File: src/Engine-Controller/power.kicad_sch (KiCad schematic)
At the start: 32 parts, among them P1 EJ508A, U2 LM22672MRE-5.0_NOPB, U3 LMS8117AMP-3.3_NOPB, U6 TPS2115APWR

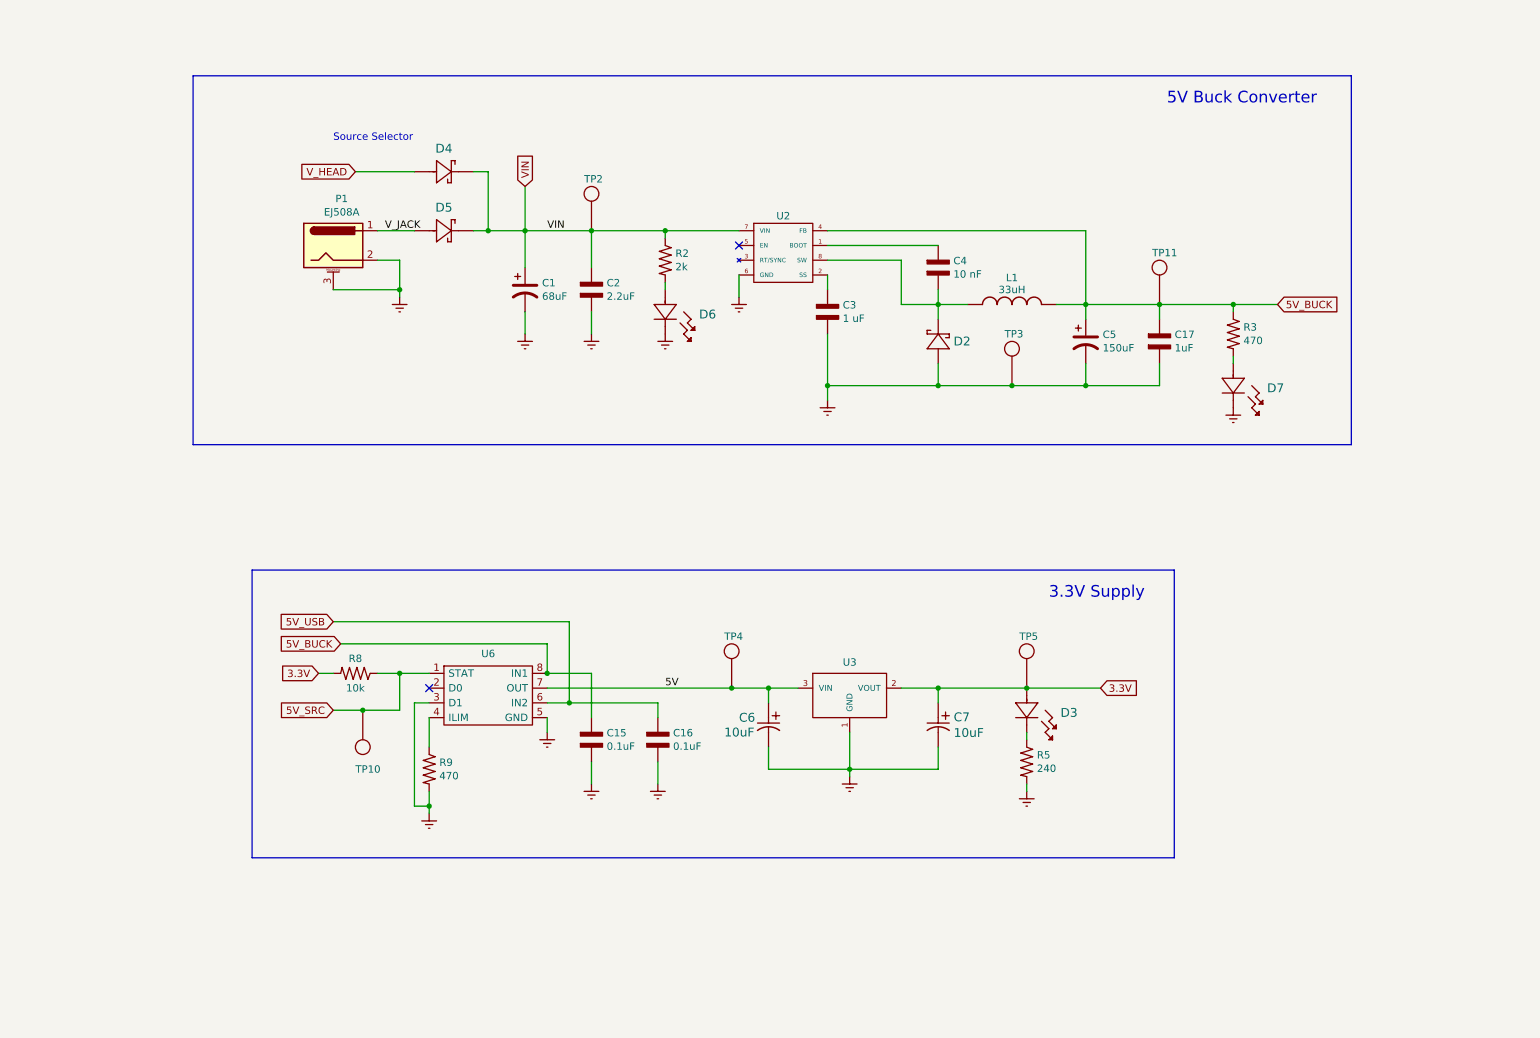
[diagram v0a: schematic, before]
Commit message: Cleaned up power schematic
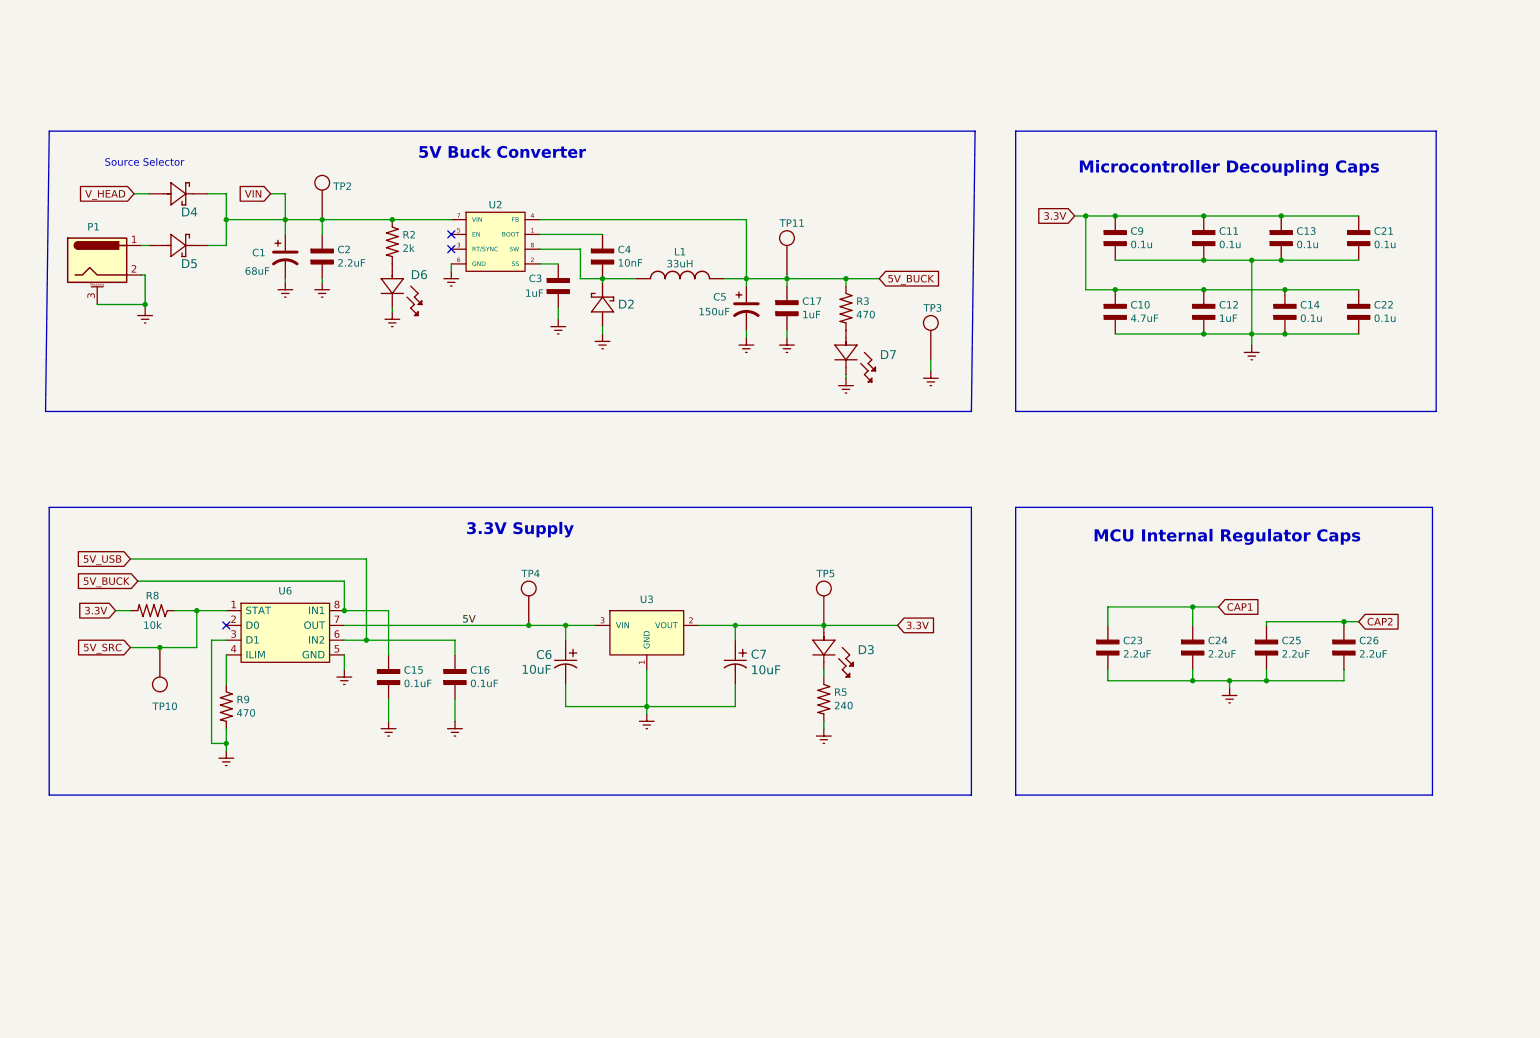
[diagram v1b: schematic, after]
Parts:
- added C10: 4.7uF, Engine-Controller:CAP_0603, symbol Engine-Controller:CAP_0603
- added C11, C13, C14, C21, C22, C9: 0.1u, Engine-Controller:CAP_0603, symbol Engine-Controller:CAP_0603
- added C12: 1uF, Engine-Controller:CAP_0603, symbol Engine-Controller:CAP_0603
- added C23, C24, C25, C26: 2.2uF, Engine-Controller:CAP_0603, symbol Engine-Controller:CAP_0603
- C3: value 1 uF -> 1uF
- C4: value 10 nF -> 10nF
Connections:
- net 3.3V: now also C10.2, C11.2, C12.2, C13.2, C14.2, C21.2, C22.2, C9.2
- net Earth: now also C10.1, C11.1, C12.1, C13.1, C14.1, C21.1, C22.1, C23.1, C24.1, C25.1, C26.1, C9.1
- net V_JACK: no longer names the net of D5.2, P1.1
- new net CAP1: C23.2, C24.2
- new net CAP2: C25.2, C26.2
- no-connect marks 2 -> 3
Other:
- note added: "MCU Internal Regulator Caps"
- note added: "Microcontroller Decoupling Caps"
- moved on the sheet: C1, C15, C16, C17, C2, C3, C4, C5, C6, C7, D2, D3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

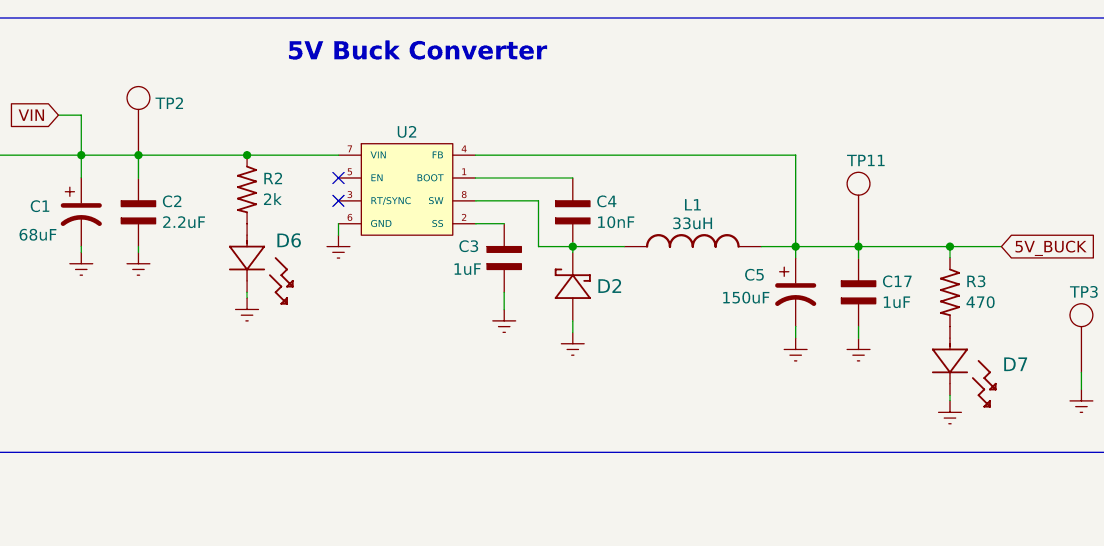
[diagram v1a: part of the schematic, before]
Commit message: adjusted power supply ceramic capacitances
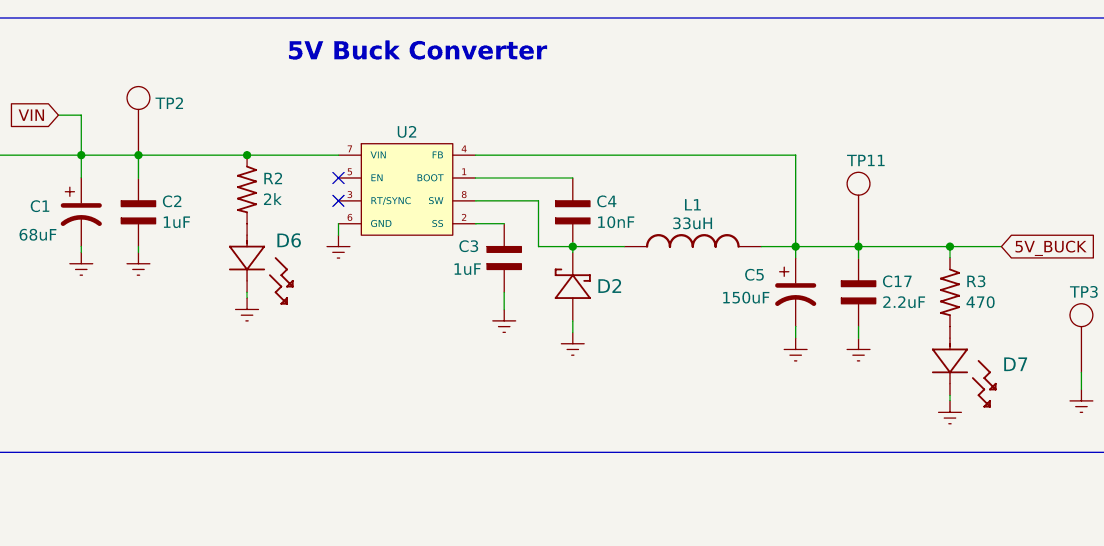
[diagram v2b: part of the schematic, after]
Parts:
- C17: value 1uF -> 2.2uF
- C2: value 2.2uF -> 1uF
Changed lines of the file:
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@@
       (effects (font (size 1.27 1.27)) (justify left))
     )
-    (property "Value" "2.2uF" (id 1) (at 74.3712 60.198 90)
+    (property "Value" "1uF" (id 1) (at 74.3712 60.198 90)
       (effects (font (size 1.27 1.27)) (justify left))
     )
@@
       (effects (font (size 1.27 1.27)) (justify left))
     )
-    (property "Value" "1uF" (id 1) (at 154.3812 69.088 90)
-      (effects (font (size 1.27 1.27)) (justify left))
-    )
+    (property "Value" "2.2uF" (id 1) (at 154.3812 69.088 90)
+      (effects (font (size 1.27 1.27)) (justify left))
+    )

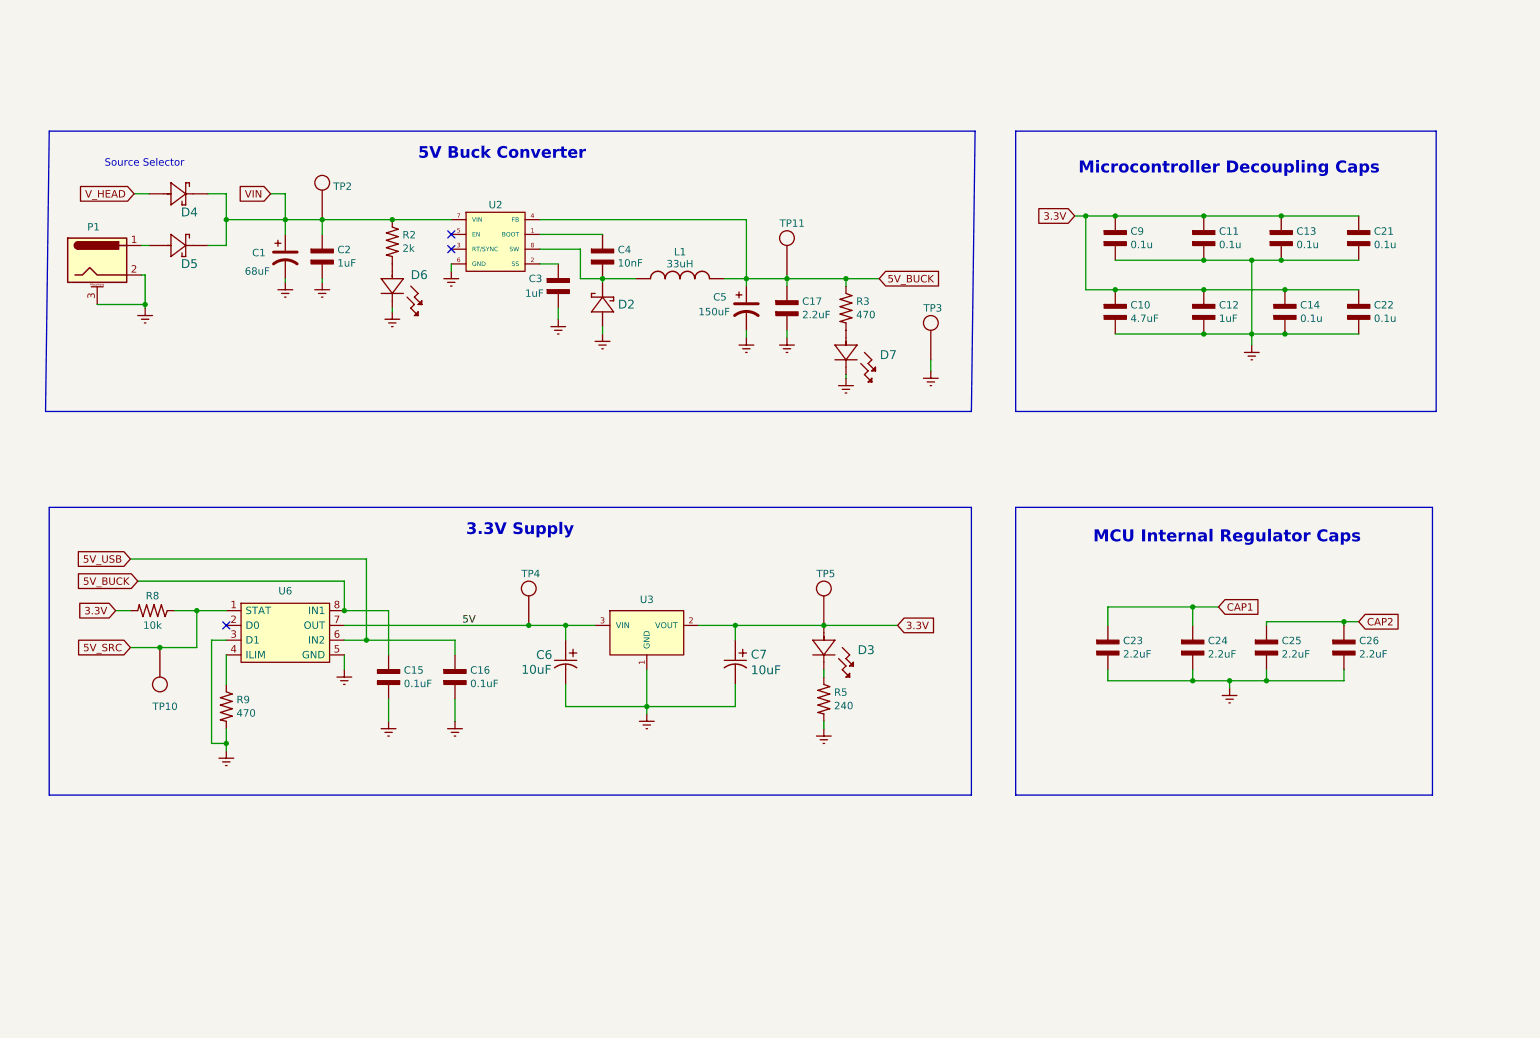
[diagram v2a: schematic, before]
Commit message: Added connectors for valve controller and main power line
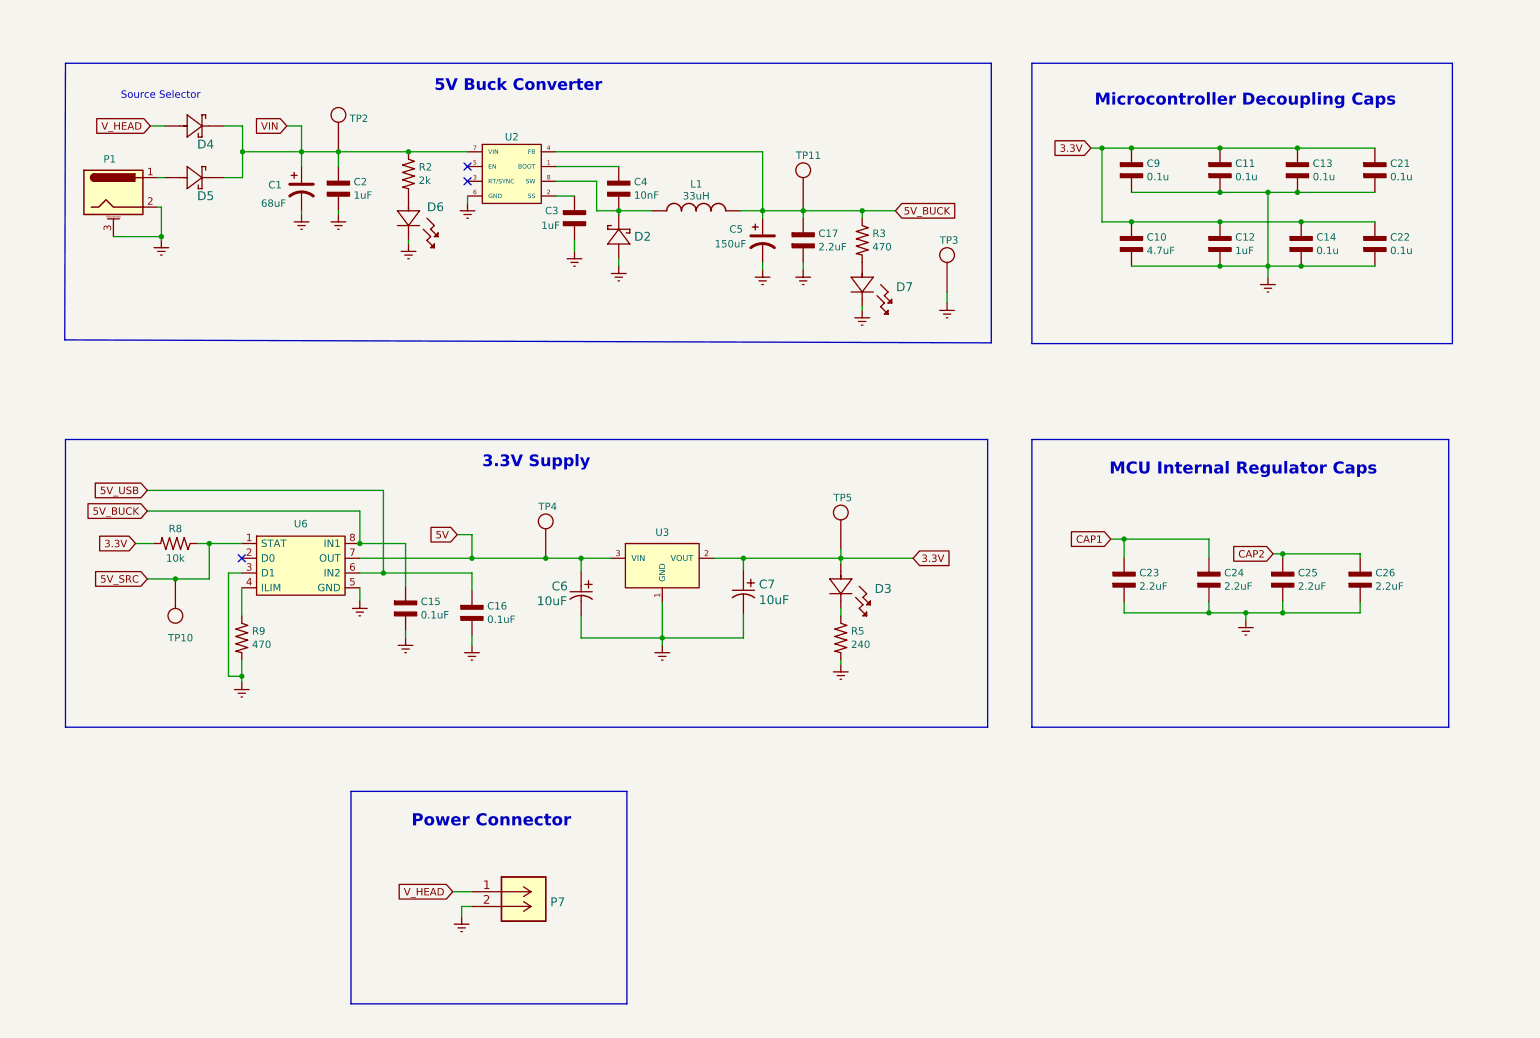
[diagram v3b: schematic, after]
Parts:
- added P7: 647676-2, CONN_2043-1X04G00DAU_OUP, symbol Engine-Controller:647676-2
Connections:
- net Earth: now also P7.2
- net V_HEAD: now also P7.1
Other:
- note added: "Power Connector"
- moved on the sheet: C1, C10, C11, C12, C13, C14, C15, C16, C17, C2, C21, C22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

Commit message: cleaned up power schematic
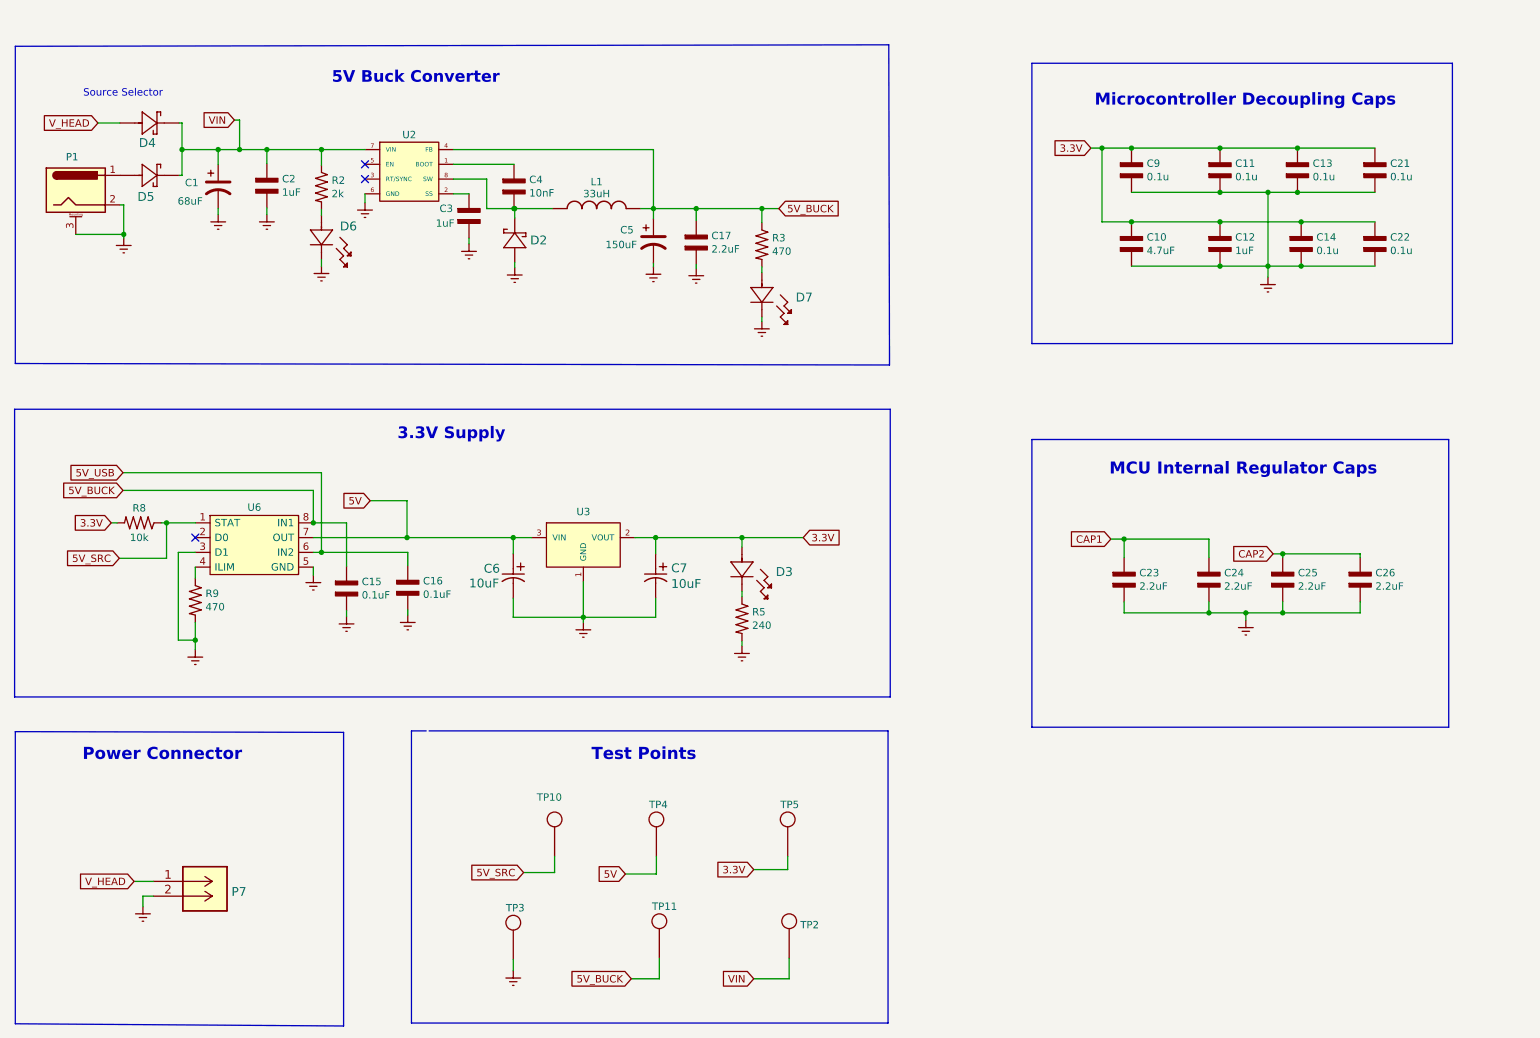
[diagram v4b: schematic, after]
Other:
- note added: "Test Points"
- moved on the sheet: C1, C15, C16, C17, C2, C3, C4, C5, C6, C7, D2, D3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
